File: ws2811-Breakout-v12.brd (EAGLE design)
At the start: 19.1 x 12.7 mm, 9 parts, among them U1 LED-TRICOLOR-5050

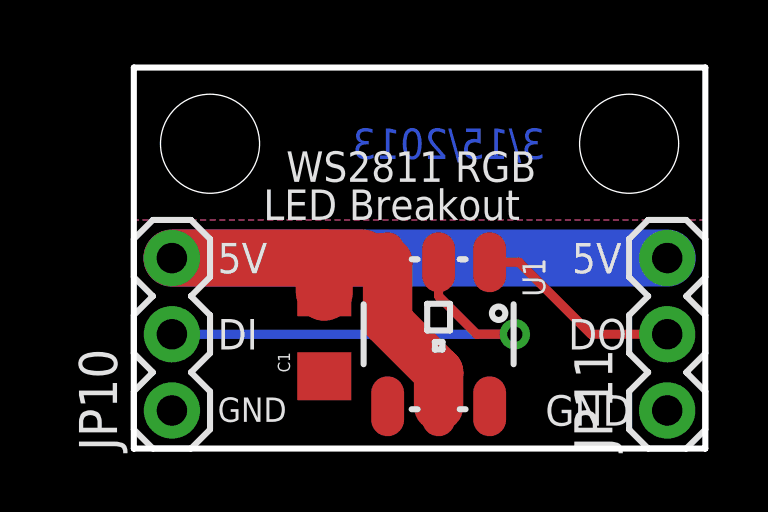
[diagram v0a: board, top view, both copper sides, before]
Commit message: Fixed all erros posed by engineers
Changed dimension to allow board to fit on .1 grid.
Changed cap value and package.
Used new frame on sch.
Centered LED.
Clean up repo.
Added version code instead of date.
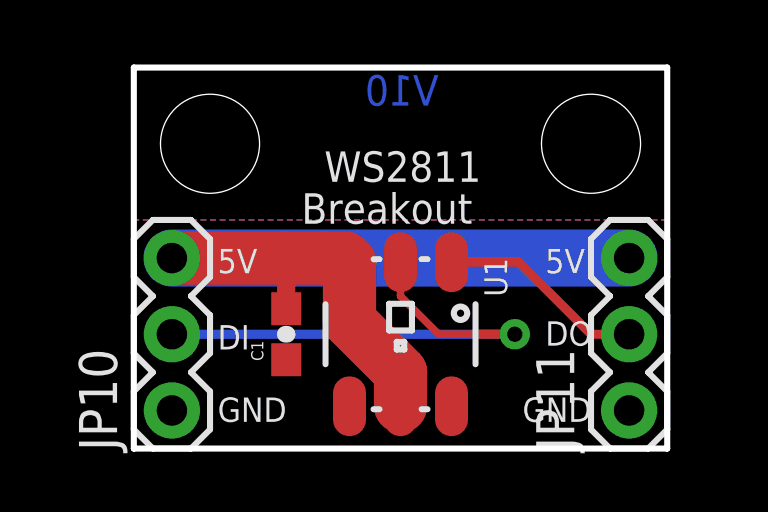
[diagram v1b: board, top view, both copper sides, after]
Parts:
- removed U$1: CREATIVE_COMMONS, SparkFun:CREATIVE_COMMONS
- added FRAME2: FRAME-LETTER, SparkFun-Aesthetics:CREATIVE_COMMONS
- C1: value 10uF -> 0.1uF; device SparkFun:1206 -> SparkFun:0603-CAP
- moved JP1 1.27 mm to (15.2, 10.2)
- moved C1 1.27 mm to (5.08, 3.81)
- moved JP11 1.27 mm to (16.5, 1.27)
- moved U1 1.27 mm to (8.89, 3.81)
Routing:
- net DI: track 15.6 -> 16.9 mm
- net VCC: track 30.4 -> 29.2 mm
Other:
- board size 19.1 x 12.7 mm -> 17.8 x 12.7 mm
- board text added: "Breakout"
- board text added: "V10"
- board text added: "WS2811"
- board text removed: "3/15/2013"
- board text removed: "LED Breakout"
- board text removed: "WS2811 RGB"
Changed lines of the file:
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@@
 <layer number="18" name="Vias" color="2" fill="1" visible="yes" active="yes"/>
 <layer number="19" name="Unrouted" color="6" fill="1" visible="yes" active="yes"/>
-<layer number="20" name="Dimension" color="6" fill="1" visible="yes" active="yes"/>
+<layer number="20" name="Dimension" color="7" fill="1" visible="yes" active="yes"/>
 <layer number="21" name="tPlace" color="16" fill="1" visible="yes" active="yes"/>
 <layer number="22" name="bPlace" color="14" fill="1" visible="yes" active="yes"/>
@@
 <plain>
 <wire x1="0" y1="0" x2="0" y2="12.7" width="0.2032" layer="20"/>
-<wire x1="0" y1="12.7" x2="19.05" y2="12.7" width="0.2032" layer="20"/>
-<wire x1="19.05" y1="12.7" x2="19.05" y2="0" width="0.2032" layer="20"/>
-<wire x1="19.05" y1="0" x2="0" y2="0" width="0.2032" layer="20"/>
-<text x="14.605" y="5.842" size="1.016" layer="21" font="vector" ratio="15">5V</text>
-<text x="2.794" y="3.302" size="1.016" layer="21" font="vector" ratio="15">DI</text>
-<text x="13.716" y="0.762" size="1.016" layer="21" font="vector" ratio="15">GND</text>
-<text x="2.794" y="5.842" size="1.016" layer="21" font="vector" ratio="15">5V</text>
-<text x="14.478" y="3.302" size="1.016" layer="21" font="vector" ratio="15">DO</text>
+<wire x1="0" y1="12.7" x2="17.78" y2="12.7" width="0.2032" layer="20"/>
+<wire x1="17.78" y1="12.7" x2="17.78" y2="0" width="0.2032" layer="20"/>
+<wire x1="17.78" y1="0" x2="0" y2="0" width="0.2032" layer="20"/>
+<text x="13.716" y="5.842" size="0.8128" layer="21" font="vector" ratio="15">5V</text>
+<text x="2.794" y="3.302" size="0.8128" layer="21" font="vector" ratio="15">DI</text>
+<text x="12.954" y="0.889" size="0.8128" layer="21" font="vector" ratio="15">GND</text>
+<text x="2.794" y="5.842" size="0.8128" layer="21" font="vector" ratio="15">5V</text>
+<text x="13.716" y="3.429" size="0.8128" layer="21" font="vector" ratio="15">DO</text>
 <text x="2.794" y="0.889" size="0.8128" layer="21" font="vector" ratio="15">GND</text>
-<text x="13.716" y="9.652" size="1.016" layer="16" ratio="20" rot="MR0">3/15/2013</text>
+<text x="10.16" y="11.43" size="1.016" layer="16" ratio="20" rot="MR0">V10</text>
 <text x="4.572" y="5.842" size="1.016" layer="22" font="vector" ratio="15" rot="MR0">5V</text>
-<text x="16.256" y="3.302" size="1.016" layer="22" font="vector" ratio="15" rot="MR0">DO</text>
+<text x="14.986" y="3.302" size="1.016" layer="22" font="vector" ratio="15" rot="MR0">DO</text>
 <text x="5.334" y="0.762" size="1.016" layer="22" font="vector" ratio="15" rot="MR0">GND</text>
-<text x="16.256" y="5.842" size="1.016" layer="22" font="vector" ratio="15" rot="MR0">5V</text>
+<text x="14.986" y="5.842" size="1.016" layer="22" font="vector" ratio="15" rot="MR0">5V</text>
 <text x="4.318" y="3.302" size="1.016" layer="22" font="vector" ratio="15" rot="MR0">DI</text>
-<text x="16.256" y="0.762" size="1.016" layer="22" font="vector" ratio="15" rot="MR0">GND</text>
-<text x="5.08" y="8.89" size="1.016" layer="21" font="vector" ratio="15">WS2811 RGB</text>
-<text x="4.318" y="7.62" size="1.016" layer="21" font="vector" ratio="15">LED Breakout</text>
-<text x="16.51" y="-8.89" size="1.778" layer="48" ratio="15">N. Seidle</text>
+<text x="14.986" y="0.762" size="1.016" layer="22" font="vector" ratio="15" rot="MR0">GND</text>
+<text x="6.35" y="8.89" size="1.016" layer="21" font="vector" ratio="15">WS2811</text>
+<text x="5.588" y="7.493" size="1.016" layer="21" font="vector" ratio="15">Breakout</text>
+<text x="17.78" y="-17.78" size="1.778" layer="48" ratio="15">N. Seidle</text>
 </plain>
 <attributes>
@@
 </autorouter>
 <elements>
-<element name="C1" library="SparkFun" package="1206" value="10uF" x="6.35" y="3.81" rot="R90"/>
+<element name="C1" library="SparkFun" package="0603-CAP" value="0.1uF" x="5.08" y="3.81" rot="R90"/>
 <element name="JP3" library="SparkFun" package="SFE-LOGO-FLAME" value="LOGO-SFESK" x="11.049" y="2.54" rot="MR0"/>
-<element name="U$1" library="SparkFun" package="CREATIVE_COMMONS" value="CREATIVE_COMMONS" x="-13.97" y="-8.89"/>
-<element name="JP1" library="SparkFun" package="STAND-OFF" value="STAND-OFF" x="16.51" y="10.16"/>
+<element name="JP1" library="SparkFun" package="STAND-OFF" value="STAND-OFF" x="15.24" y="10.16"/>
 <element name="JP4" library="SparkFun" package="STAND-OFF" value="STAND-OFF" x="2.54" y="10.16"/>
-<element name="U1" library="SparkFun-LED" package="LED-TRICOLOR-5050-IC" value="LED-TRICOLOR-5050" x="10.16" y="3.81" rot="R270"/>
+<element name="U1" library="SparkFun-LED" package="LED-TRICOLOR-5050-IC" value="LED-TRICOLOR-5050" x="8.89" y="3.81" rot="R270"/>
 <element name="JP10" library="SparkFun-Connectors" package="1X03" value="INPUT" x="1.27" y="1.27" rot="R90"/>
-<element name="JP11" library="SparkFun-Connectors" package="1X03" value="OUTPUT" x="17.78" y="1.27" rot="R90"/>
+<element name="JP11" library="SparkFun-Connectors" package="1X03" value="OUTPUT" x="16.51" y="1.27" rot="R90"/>
 <element name="LOGO1" library="SparkFun-Aesthetics" package="OSHW-LOGO-S" value="OSHW-LOGOS" x="6.35" y="3.81" rot="MR0"/>
+<element name="FRAME2" library="SparkFun-Aesthetics" package="CREATIVE_COMMONS" value="FRAME-LETTER" x="-13.97" y="-17.78"/>
 </elements>
 <signals>
@@
 <contactref element="JP10" pad="3"/>
 <contactref element="JP11" pad="3"/>
-<wire x1="17.78" y1="6.35" x2="1.27" y2="6.35" width="1.905" layer="16"/>
-<wire x1="1.27" y1="6.35" x2="6.35" y2="6.35" width="1.905" layer="1"/>
-<wire x1="6.35" y1="6.35" x2="7.62" y2="6.35" width="1.905" layer="1"/>
-<wire x1="6.35" y1="5.21" x2="6.35" y2="6.35" width="1.905" layer="1"/>
-<wire x1="7.62" y1="6.35" x2="8.128" y2="6.35" width="1.27" layer="1"/>
-<wire x1="10.16" y1="1.41" x2="10.16" y2="2.54" width="1.651" layer="1"/>
-<wire x1="10.16" y1="2.54" x2="8.46" y2="4.24" width="1.651" layer="1"/>
-<wire x1="8.46" y1="6.21" x2="8.46" y2="4.24" width="1.651" layer="1"/>
-<wire x1="8.128" y1="6.35" x2="8.32" y2="6.35" width="1.651" layer="1"/>
-<wire x1="8.32" y1="6.35" x2="8.46" y2="6.21" width="1.651" layer="1"/>
+<wire x1="16.51" y1="6.35" x2="1.27" y2="6.35" width="1.905" layer="16"/>
+<wire x1="7.112" y1="6.35" x2="7.19" y2="6.21" width="0.254" layer="1"/>
+<wire x1="1.27" y1="6.35" x2="5.08" y2="6.35" width="1.778" layer="1"/>
+<wire x1="5.08" y1="6.35" x2="6.35" y2="6.35" width="1.778" layer="1"/>
+<wire x1="6.35" y1="6.35" x2="7.05" y2="6.35" width="1.778" layer="1"/>
+<wire x1="7.19" y1="6.21" x2="7.19" y2="4.24" width="1.778" layer="1"/>
+<wire x1="8.89" y1="1.41" x2="8.89" y2="2.54" width="1.778" layer="1"/>
+<wire x1="8.89" y1="2.54" x2="7.19" y2="4.24" width="1.778" layer="1"/>
+<wire x1="7.19" y1="6.21" x2="6.35" y2="6.35" width="1.778" layer="1"/>
+<wire x1="5.08" y1="4.66" x2="5.08" y2="6.35" width="0.6096" layer="1"/>
 </signal>
 <signal name="GND">
@@
 <vertex x="0" y="7.62"/>
 <vertex x="0" y="0"/>
-<vertex x="19.05" y="0"/>
-<vertex x="19.05" y="7.62"/>
+<vertex x="17.78" y="0"/>
+<vertex x="17.78" y="7.62"/>
 </polygon>
 <polygon width="0.254" layer="16" isolate="0.3048">
 <vertex x="0" y="7.62"/>
 <vertex x="0" y="0"/>
-<vertex x="19.05" y="0"/>
-<vertex x="19.05" y="7.62"/>
+<vertex x="17.78" y="0"/>
+<vertex x="17.78" y="7.62"/>
 </polygon>
 <contactref element="U1" pad="6"/>
@@
 <contactref element="JP11" pad="2"/>
 <contactref element="U1" pad="1"/>
-<wire x1="11.86" y1="6.21" x2="12.84" y2="6.21" width="0.3048" layer="1"/>
+<wire x1="10.59" y1="6.21" x2="12.84" y2="6.21" width="0.3048" layer="1"/>
 <wire x1="12.84" y1="6.21" x2="15.24" y2="3.81" width="0.3048" layer="1"/>
-<wire x1="15.24" y1="3.81" x2="17.78" y2="3.81" width="0.3048" layer="1"/>
+<wire x1="15.24" y1="3.81" x2="16.51" y2="3.81" width="0.3048" layer="1"/>
 </signal>
 <signal name="DI">
 <contactref element="U1" pad="2" route="any" routetag="DI"/>
 <contactref element="JP10" pad="2"/>
-<wire x1="10.16" y1="6.21" x2="10.16" y2="5.08" width="0.3048" layer="1"/>
-<wire x1="10.16" y1="5.08" x2="11.43" y2="3.81" width="0.3048" layer="1"/>
 <wire x1="11.43" y1="3.81" x2="12.7" y2="3.81" width="0.3048" layer="1"/>
 <via x="12.7" y="3.81" extent="1-16" drill="0.508"/>
 <wire x1="12.7" y1="3.81" x2="1.27" y2="3.81" width="0.3048" layer="16"/>
+<wire x1="8.89" y1="6.21" x2="8.89" y2="5.08" width="0.254" layer="1"/>
+<wire x1="8.89" y1="5.08" x2="10.16" y2="3.81" width="0.254" layer="1"/>
+<wire x1="10.16" y1="3.81" x2="11.43" y2="3.81" width="0.254" layer="1"/>
 </signal>
 </signals>
